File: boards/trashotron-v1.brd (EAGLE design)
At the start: 88.9 x 50.8 mm, 6 parts, among them IC1 MCP604P, IC2 MCP604P, J3 455-1750-1-ND

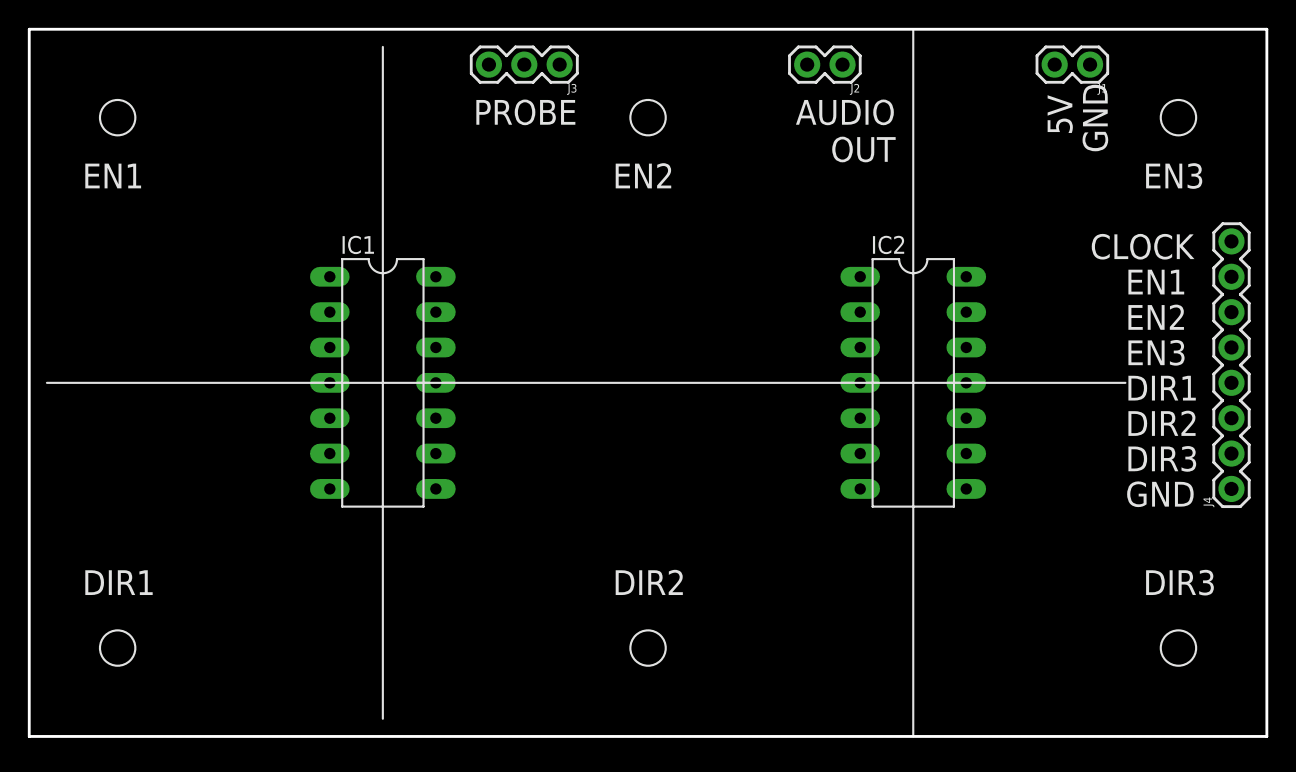
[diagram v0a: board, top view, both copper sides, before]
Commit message: trashotron board mostly laid out in schematic
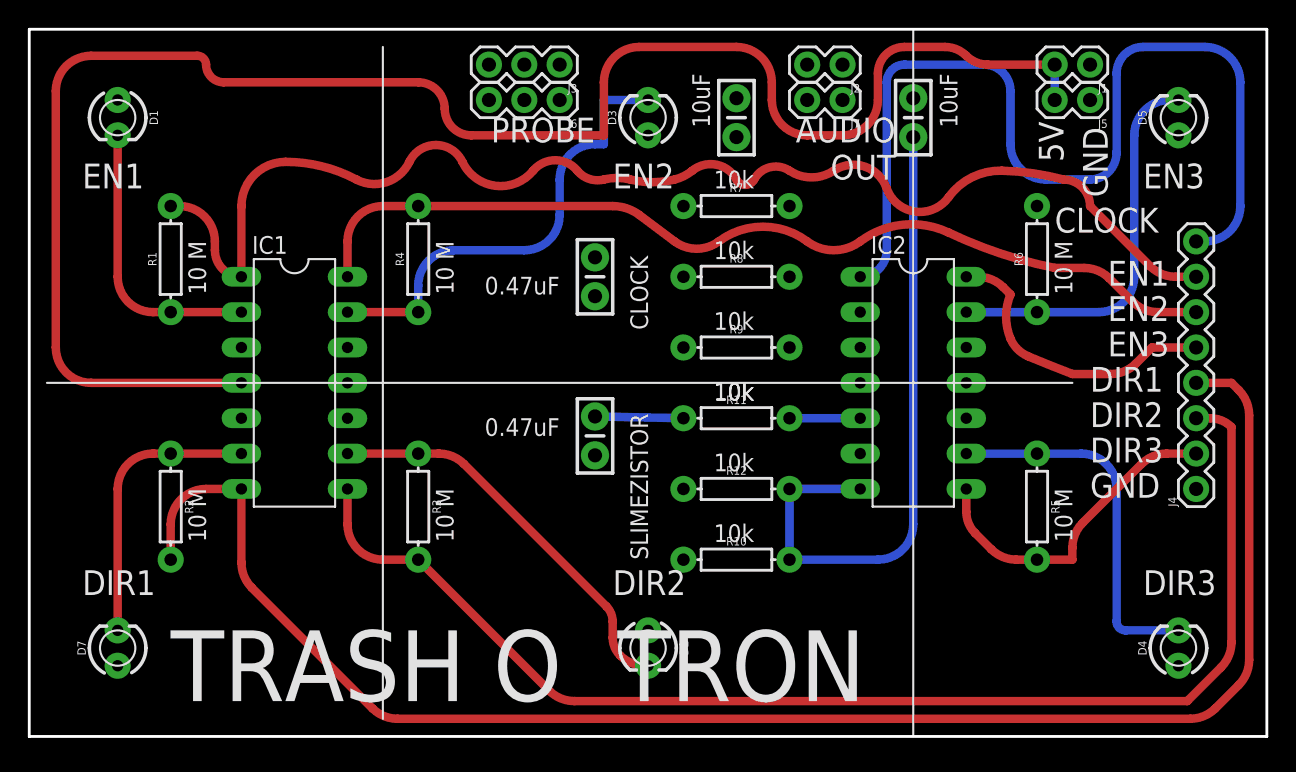
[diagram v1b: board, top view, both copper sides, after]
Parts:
- added C1, C2, C3, C4: 0.1uF, SparkFun-Capacitors:CAP-PTH-SMALL-KIT
- added D1, D2, D3, D4, D5, D7: (no value), SparkFun-LED:LED_3MM
- added J5, J7: (no value), SparkFun-Connectors:1X02
- added J6: 455-1750-1-ND, SparkFun-Connectors:1X03
- added R1, R10, R11, R12, R2, R3, R4, R5, R6, R7, R8, R9: (no value), SparkFun-Resistors:AXIAL-0.3
- moved IC1 6.35 mm to (19.1, 25.4)
- moved J4 2.54 mm to (83.8, 17.8)
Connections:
- removed net V+: IC1.4, IC2.4
- removed net V-: IC1.11, IC2.11
- new net AUDIO+: C3.2, J2.1, J7.1
- new net AUDIO-: C4.2, J2.2, J7.2
- new net CLOCK: IC2.1, J4.8, R7.P$2, R8.P$2
- new net DIR1: IC1.7, J4.4, R2.P$2
- new net DIR2: IC1.8, J4.3, R3.P$2
- new net DIR3: IC2.8, J4.2, R5.P$2
- new net EN1: IC1.1, J4.7, R1.P$2
- new net EN2: IC1.14, J4.6, R4.P$2
- new net EN3: IC2.14, J4.5, R6.P$2
- new net GND: C1.2, C2.2, C4.1, D1.A, D2.A, D3.A, D4.A, D5.A, D7.A, IC1.10, IC1.11, IC1.12, IC1.3, IC1.5, IC2.10, IC2.11, J1.1, J3.3, J4.1, J5.1, J6.3
- new net N$1: D1.K, IC1.2, R1.P$1
- new net N$11: D5.K, IC2.13, R6.P$1
- new net N$13: D3.K, IC1.13, R4.P$1
- new net N$15: C2.1, IC2.6, J3.2, J6.2, R11.P$1, R12.P$1
- new net N$16: IC2.3, R8.P$1, R9.P$2
- new net N$18: IC2.5, R10.P$1, R11.P$2
- new net N$19: IC1.4, IC2.4, J1.2, J5.2
- new net N$24: C1.1, IC2.2, R7.P$1, R9.P$1
- new net N$25: C3.1, IC2.7, J3.1, J6.1, R10.P$2, R12.P$2
- new net N$5: D7.K, IC1.6, R2.P$1
- new net N$7: D2.K, IC1.9, R3.P$1
- new net N$9: D4.K, IC2.9, R5.P$1
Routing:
- net N$19: track 0.00 -> 122.8 mm
- net DIR1: track 0.00 -> 116.2 mm
- net DIR2: track 0.00 -> 91.5 mm
- net EN1: track 0.00 -> 86.8 mm
- net CLOCK: track 0.00 -> 67.8 mm
- net EN2: track 0.00 -> 66.7 mm
- net N$25: track 0.00 -> 47.9 mm
- net N$13: track 0.00 -> 32.4 mm
- net N$7: track 0.00 -> 28.9 mm
- net N$11: track 0.00 -> 27.5 mm
- net N$9: track 0.00 -> 26.1 mm
- net DIR3: track 0.00 -> 23.8 mm
- net EN3: track 0.00 -> 21.5 mm
- net N$5: track 0.00 -> 20.1 mm
- net N$1: track 0.00 -> 20.1 mm
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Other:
- board text added: "0.47uF"
- board text added: "10 M"
- board text added: "10k"
- board text added: "10uF"
- board text added: "SLIMEZISTOR"
- board text added: "TRASH O TRON"
